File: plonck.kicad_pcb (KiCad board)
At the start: 2 copper layers, 228.6 x 78.7 mm, 127 parts, among them J1 Battery_connector, Q1 Q_PMOS_DSG, SW1 SW_Push, U1 SRV05-4, U2 TP4054-42-SOT25-R, U3 XC6206PxxxMR-Regulator_Linear, U4 nRF52840_holyiot_18010, q1 USB4085-GF-A_REVA

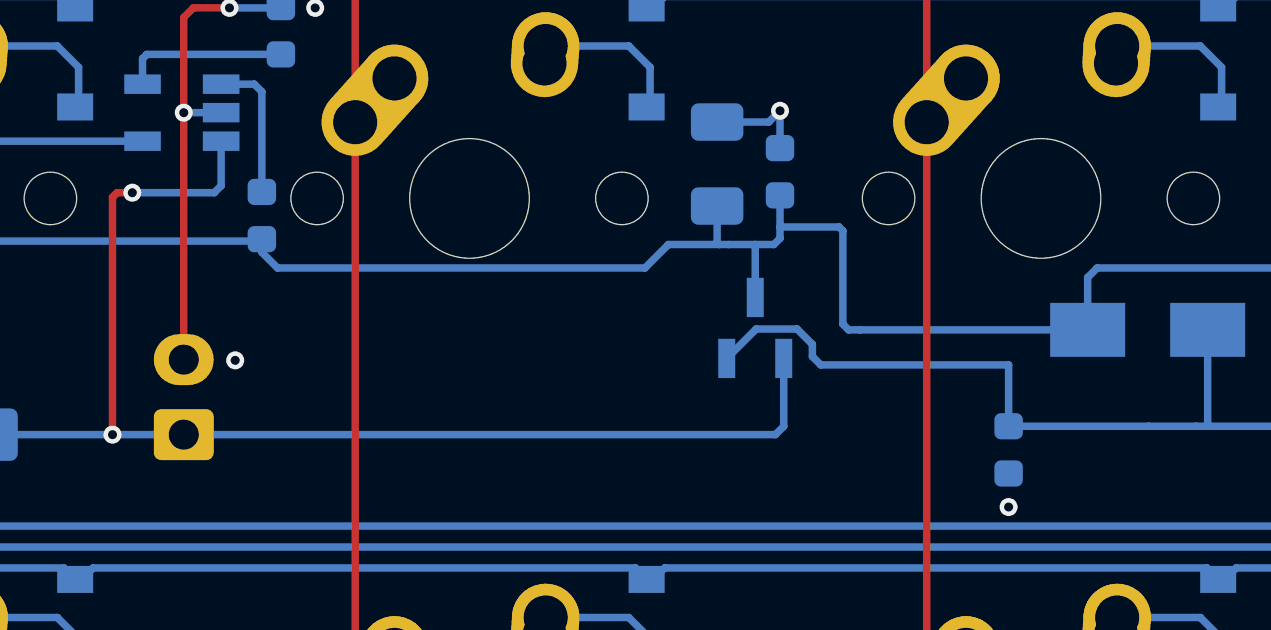
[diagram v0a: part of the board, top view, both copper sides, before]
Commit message: fixed incorrect schematic symbol for mosfet
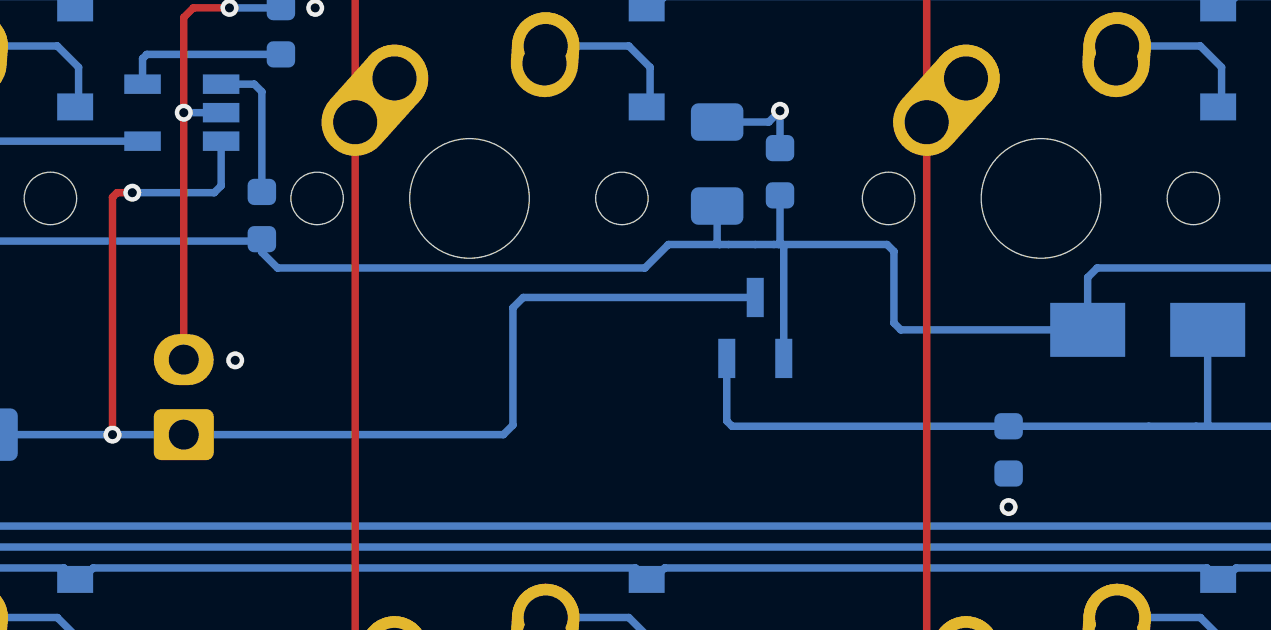
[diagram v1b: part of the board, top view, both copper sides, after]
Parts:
- Q1: value Q_PMOS_DSG -> Q_PMOS_GSD
- renumbered DEBUG to J2
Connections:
- Q1 pad 1: +BATT -> VBUS
- Q1 pad 3: VBUS -> +BATT
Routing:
- net VBUS: track 221.4 -> 222.9 mm
- net Net-(C5-Pad1): track 25.5 -> 24.5 mm
- net +BATT: track 41.7 -> 42.6 mm

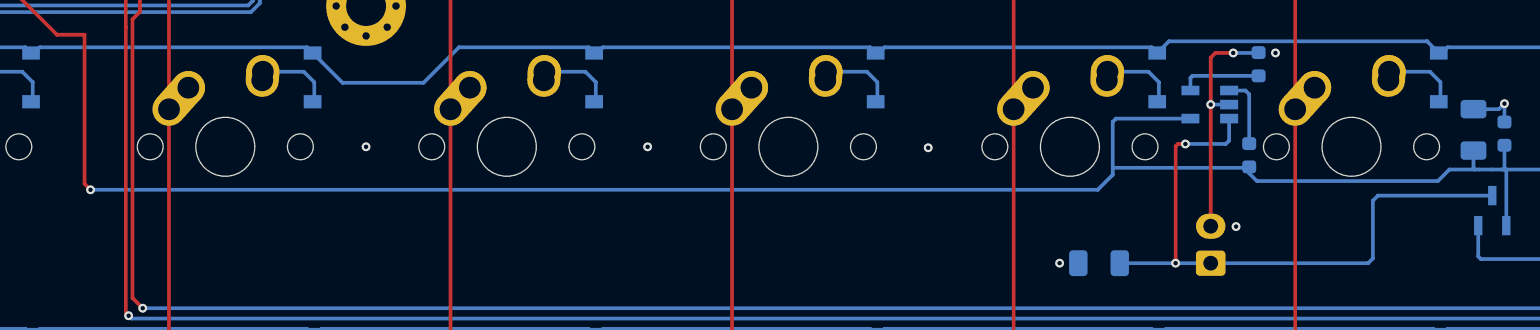
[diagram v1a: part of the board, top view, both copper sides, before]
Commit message: added charge status led
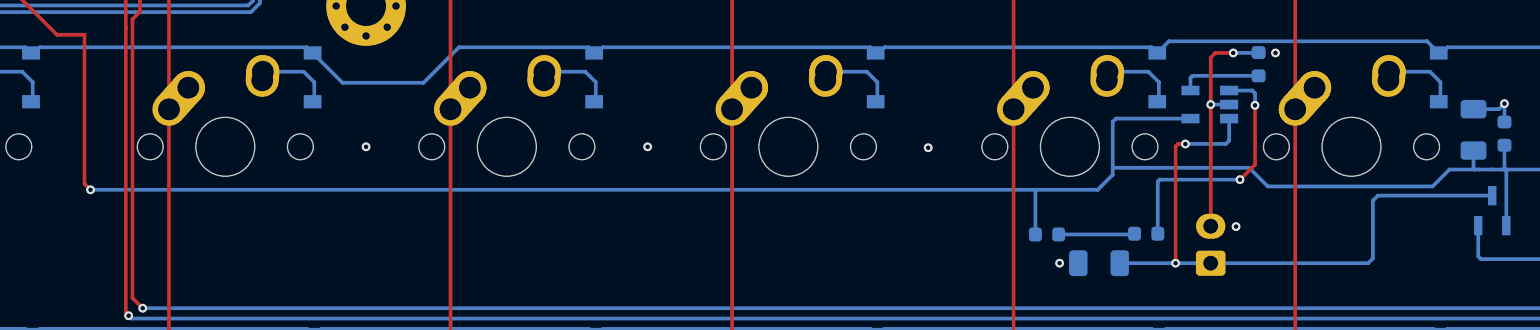
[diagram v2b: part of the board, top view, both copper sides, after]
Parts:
- added D50: KT-0603R, LED_SMD:LED_0603_1608Metric, B.Cu at (141.7, 58.3)
- moved R3 14.7 mm to (135.0, 58.3), turned to 0 degrees
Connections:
- R3 pad 2: Net-(R3-Pad2) -> Net-(D50-Pad2)
- U2 pad 1: Net-(R3-Pad2) -> Net-(D50-Pad1)
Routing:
- net Net-(D50-Pad1): track 0.00 -> 17.2 mm, vias 0 -> 2
- net Net-(D50-Pad2): track 0.00 -> 5.15 mm
- net Net-(R3-Pad2): track 4.80 -> 0.00 mm
- net VBUS: track 222.9 -> 226.0 mm

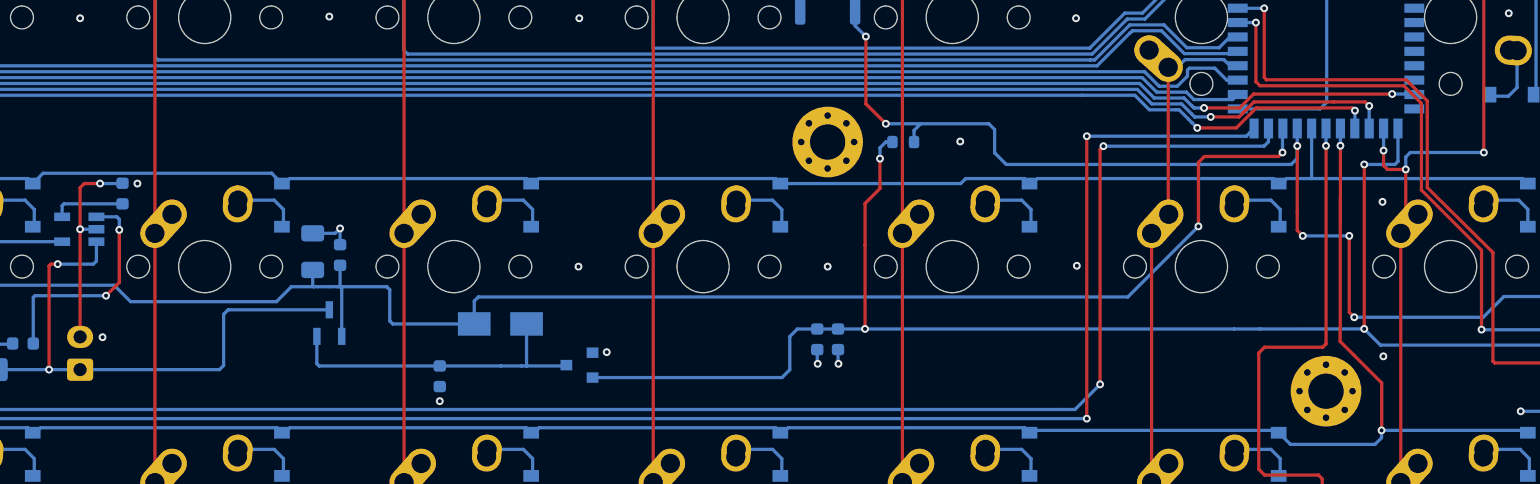
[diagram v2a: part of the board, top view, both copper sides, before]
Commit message: added vsense circuitry
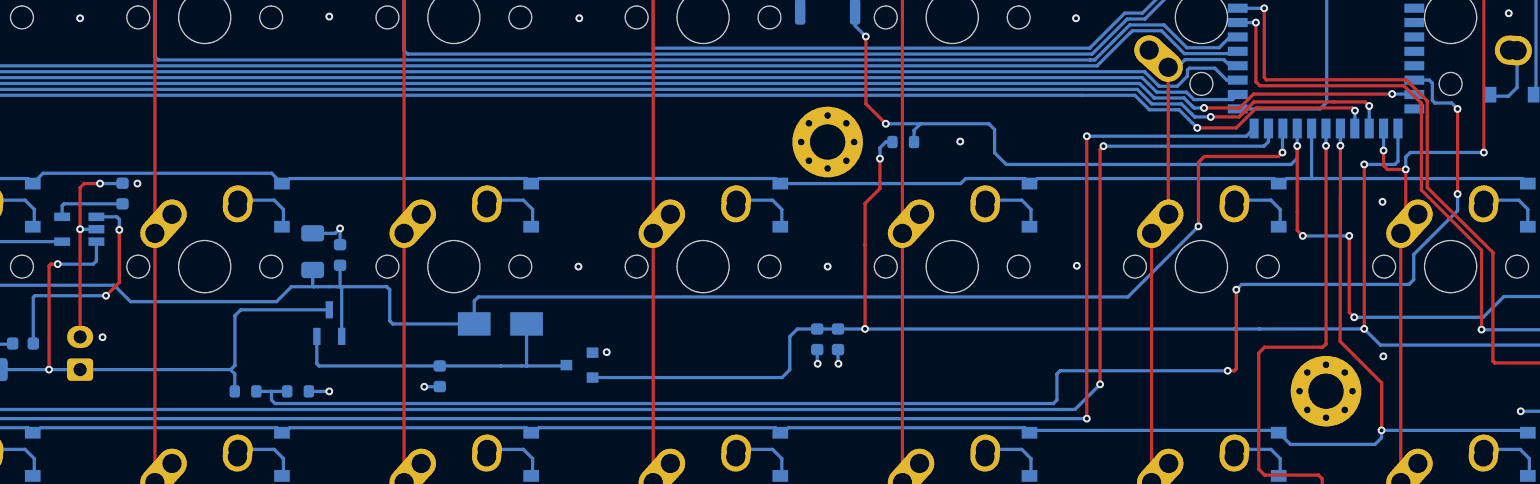
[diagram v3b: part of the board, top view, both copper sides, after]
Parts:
- added R7: 806k, Resistor_SMD:R_0603_1608Metric, B.Cu at (158.7, 61.9)
- added R8: 2M, Resistor_SMD:R_0603_1608Metric, B.Cu at (162.7, 61.9)
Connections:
- U4 pad 11: Net-(U4-Pad11) -> VSENSE
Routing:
- net VSENSE: track 0.00 -> 118.5 mm, vias 0 -> 4
- net GND: track 54.4 -> 57.2 mm, vias 84 -> 85
- net +BATT: track 42.6 -> 44.3 mm

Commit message: updated resistor values in battery voltage divider
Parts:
- R7: value 806k -> 1.2k
- R8: value 2M -> 3k

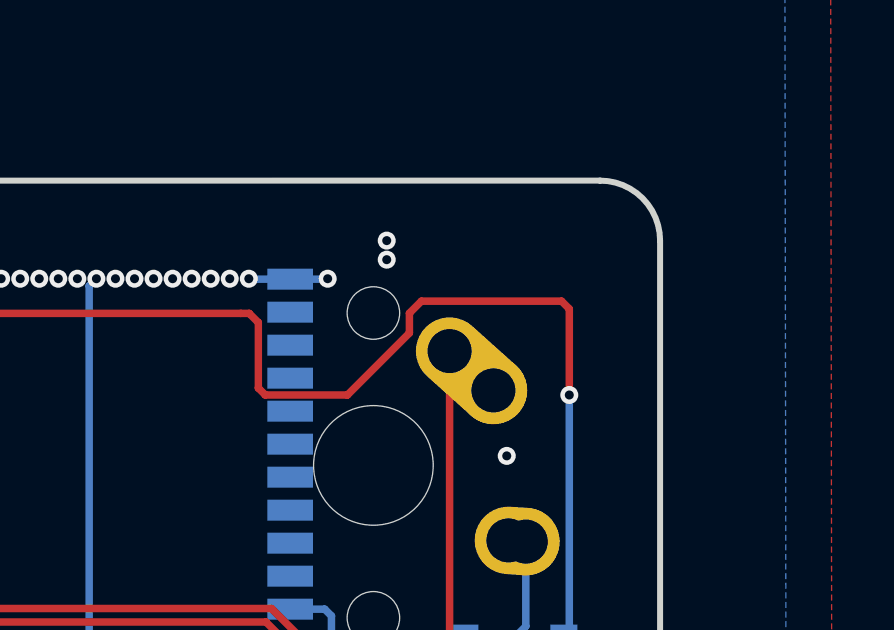
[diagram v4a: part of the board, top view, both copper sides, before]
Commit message: added bootloader status led
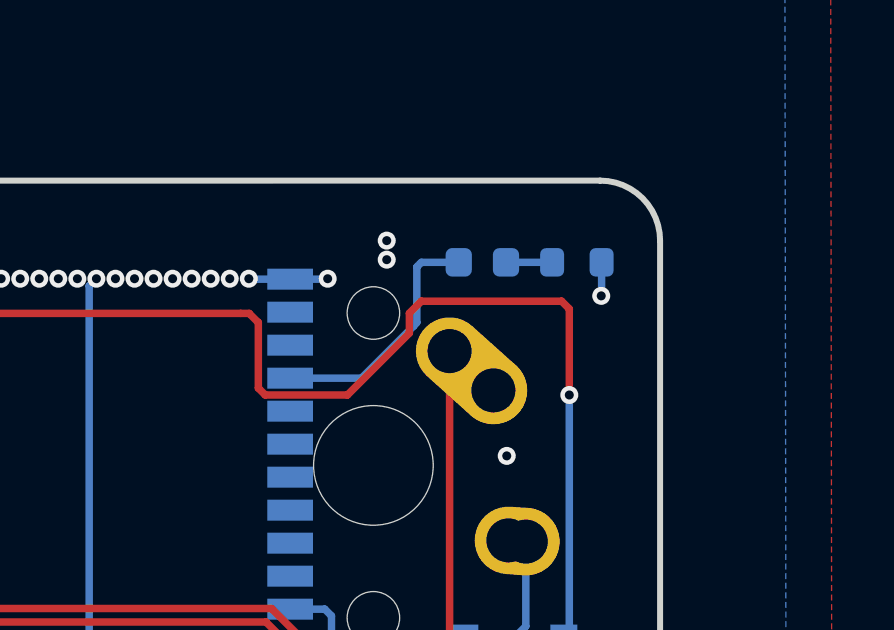
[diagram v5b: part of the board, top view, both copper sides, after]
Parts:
- added D51: 19-217/BHC-ZL1M2RY/3T, LED_SMD:LED_0603_1608Metric, B.Cu at (254.5, 26.6)
- added R9: 33, Resistor_SMD:R_0603_1608Metric, B.Cu at (257.6, 26.6)
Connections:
- U4 pad 4: Net-(U4-Pad4) -> BL_Led
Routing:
- net BL_Led: track 0.00 -> 8.31 mm
- net Net-(D51-Pad1): track 0.00 -> 1.54 mm
- net GND: track 57.2 -> 58.3 mm, vias 85 -> 86

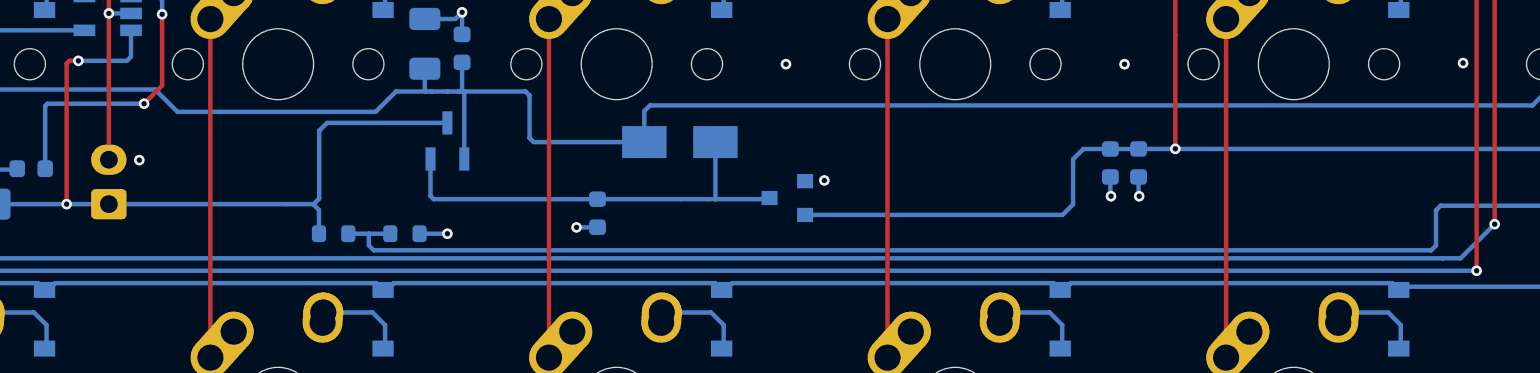
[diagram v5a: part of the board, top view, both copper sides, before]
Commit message: updated resistor values for vsense
https://devzone.nordicsemi.com/nordic/nordic-blog/b/blog/posts/measuring-lithium-battery-voltage-with-nrf52
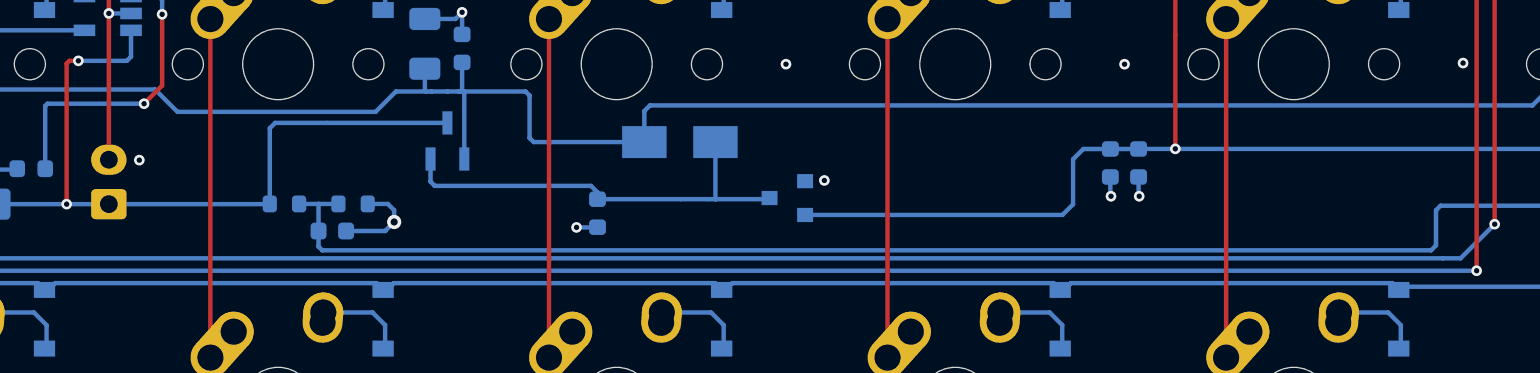
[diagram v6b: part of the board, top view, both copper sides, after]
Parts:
- added C6: 10nf, Capacitor_SMD:C_0603_1608Metric, B.Cu at (158.6, 61.8)
- moved R8 3.37 mm to (159.8, 60.2)
- moved R7 3.24 mm to (155.9, 60.2)
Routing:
- net VSENSE: track 118.5 -> 122.9 mm
- net GND: track 58.3 -> 61.9 mm
- net +BATT: track 44.3 -> 42.8 mm

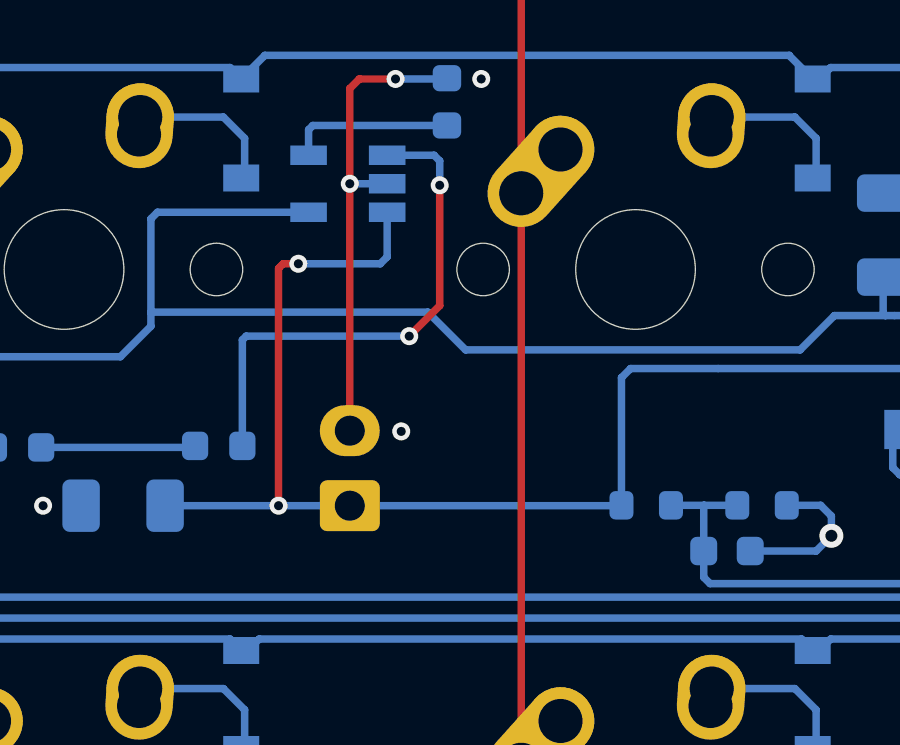
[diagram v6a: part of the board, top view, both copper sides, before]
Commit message: changed battery connector to smaller size
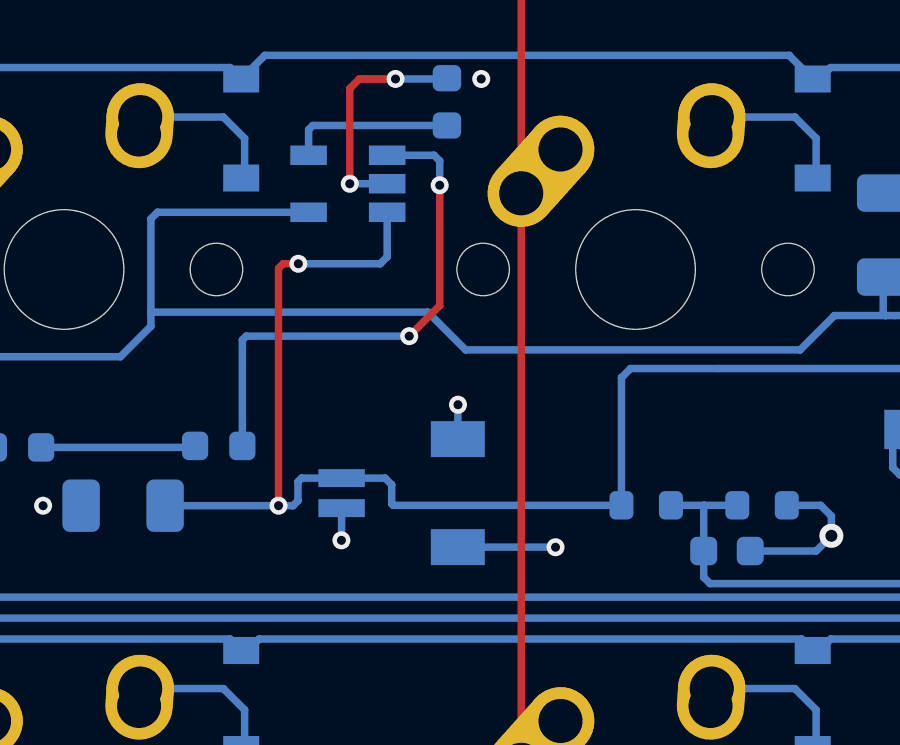
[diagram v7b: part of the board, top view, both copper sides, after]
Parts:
- J1: footprint Connector_JST:JST_EH_S2B-EH_1x02_P2.50mm_Horizontal -> SM02B-SRSS-TB_LF__SN_:SM02B-SRSS-TB(LF)(SN)
- moved J1 1.75 mm to (147.8, 59.8), turned to 270 degrees
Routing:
- net GND: track 61.9 -> 59.2 mm, vias 86 -> 88
- net +BATT: track 42.8 -> 44.3 mm

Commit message: bunch of updates and fixes related to new kicad version
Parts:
- removed C6: 10nf, Capacitor_SMD:C_0603_1608Metric
- R8: renamed from R7; value 1.2k -> 806k
- R9: renamed from R8; value 3k -> 2M
- moved C3 0.32 mm to (204.2, 58.2)
- moved C4 0.31 mm to (202.2, 58.2)
- renumbered D50 to D37, D37 to D38, D38 to D39, D39 to D40, D40 to D41, D41 to D42, D42 to D43, D43 to D44, D44 to D45, D45 to D46, D46 to D47, D47 to D48, D48 to D49, D49 to D50, H5 to H2, H2 to H3, H6 to H4, H3 to H5, H4 to H6, q1 to Q1, Q1 to Q2, R9 to R7, U4 to U3, U3 to U4
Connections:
- Q1 pad A8: Net-(q1-PadA8) -> unconnected-(Q1-PadA8)
- Q1 pad B8: Net-(q1-PadB8) -> unconnected-(Q1-PadB8)
- U1 pad 3: Net-(U1-Pad3) -> unconnected-(U1-Pad3)
- U1 pad 4: Net-(U1-Pad4) -> unconnected-(U1-Pad4)
- U3 pad 10: Net-(U4-Pad10) -> unconnected-(U3-Pad10)
- U3 pad 13: Net-(U4-Pad13) -> unconnected-(U3-Pad13)
- U3 pad 2: Net-(U4-Pad2) -> unconnected-(U3-Pad2)
- U3 pad 3: Net-(U4-Pad3) -> unconnected-(U3-Pad3)
- U3 pad 5: Net-(U4-Pad5) -> unconnected-(U3-Pad5)
- U3 pad 6: Net-(U4-Pad6) -> unconnected-(U3-Pad6)
- U3 pad 7: Net-(U4-Pad7) -> unconnected-(U3-Pad7)
- U3 pad 8: Net-(U4-Pad8) -> unconnected-(U3-Pad8)
- U3 pad 9: Net-(U4-Pad9) -> unconnected-(U3-Pad9)
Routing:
- net GND: track 59.2 -> 54.1 mm, vias 88 -> 86
- net +3V3: track 117.7 -> 118.2 mm
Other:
- net class Default removed
- net class JLCPCB removed
